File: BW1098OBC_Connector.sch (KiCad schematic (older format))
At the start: 50 parts

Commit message: Cleaned up some duplicates, started reorganizing and putting symbols into one luxonis library so the others can be deleted, added SOM Connector footprint
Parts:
- J?: symbol BW1098OBC_Connector-cache:DF40HC(3.0)-100DS-0.4V_BW1099_G2 -> BW1098OBC_TopLevel-rescue:DF40HC(3.0)-100DS-0.4V_BW1099_G2-BW1098OBC_Connector-cache
- J? (x3): symbol BW1098OBC_Connector-cache:20021121-00010T1LF -> BW1098OBC_TopLevel-rescue:20021121-00010T1LF-BW1098OBC_Connector-cache
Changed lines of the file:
@@
 $Descr B 17000 11000
 encoding utf-8
-Sheet 7 8
+Sheet 6 8
 Title "BW1098OBC_Connector-SchDoc"
 Date "14 12 2020"
@@
 2485_PGOOD and MODULE_nRST both have pull ups to 1.8V \non 1099 module. 2485_PGOOD is held low by open-drain output \non 1099 PMIC until power is good. MODULE_nRST rises with \n1.8V at POR, but can be held low by user button or 1099 JTAG.
 $Comp
-L BW1098OBC_Connector-cache:20021121-00010T1LF J?
+L BW1098OBC_TopLevel-rescue:20021121-00010T1LF-BW1098OBC_Connector-cache J?
 U 1 1 605FCE0C
 P 4250 9550
+AR Path="/605FCE0C" Ref="J?"  Part="1"
+AR Path="/5FD7EFCD/605FCE0C" Ref="J?"  Part="1"
 F 0 "J?" H 4650 9700 60  0000 C CNN
 F 1 "20021121-00010T1LF" H 4800 9000 60  0000 C CNN
@@
 $EndComp
 $Comp
-L BW1098OBC_Connector-cache:20021121-00010T1LF J?
+L BW1098OBC_TopLevel-rescue:20021121-00010T1LF-BW1098OBC_Connector-cache J?
 U 1 1 605FF28B
 P 7150 9550
+AR Path="/605FF28B" Ref="J?"  Part="1"
+AR Path="/5FD7EFCD/605FF28B" Ref="J?"  Part="1"
 F 0 "J?" H 7550 9700 60  0000 C CNN
 F 1 "20021121-00010T1LF" H 7750 9000 60  0000 C CNN
@@
 $EndComp
 $Comp
-L BW1098OBC_Connector-cache:20021121-00010T1LF J?
+L BW1098OBC_TopLevel-rescue:20021121-00010T1LF-BW1098OBC_Connector-cache J?
 U 1 1 6060E6D4
 P 10200 9550
+AR Path="/6060E6D4" Ref="J?"  Part="1"
+AR Path="/5FD7EFCD/6060E6D4" Ref="J?"  Part="1"
 F 0 "J?" H 10650 9700 60  0000 C CNN
 F 1 "20021121-00010T1LF" H 10800 9000 60  0000 C CNN
@@
 	13550 3800 13550 4050
 $Comp
-L BW1098OBC_Connector-cache:DF40HC(3.0)-100DS-0.4V_BW1099_G2 J?
+L BW1098OBC_TopLevel-rescue:DF40HC(3.0)-100DS-0.4V_BW1099_G2-BW1098OBC_Connector-cache J?
 U 1 1 5FDB88CE
 P 7350 2000

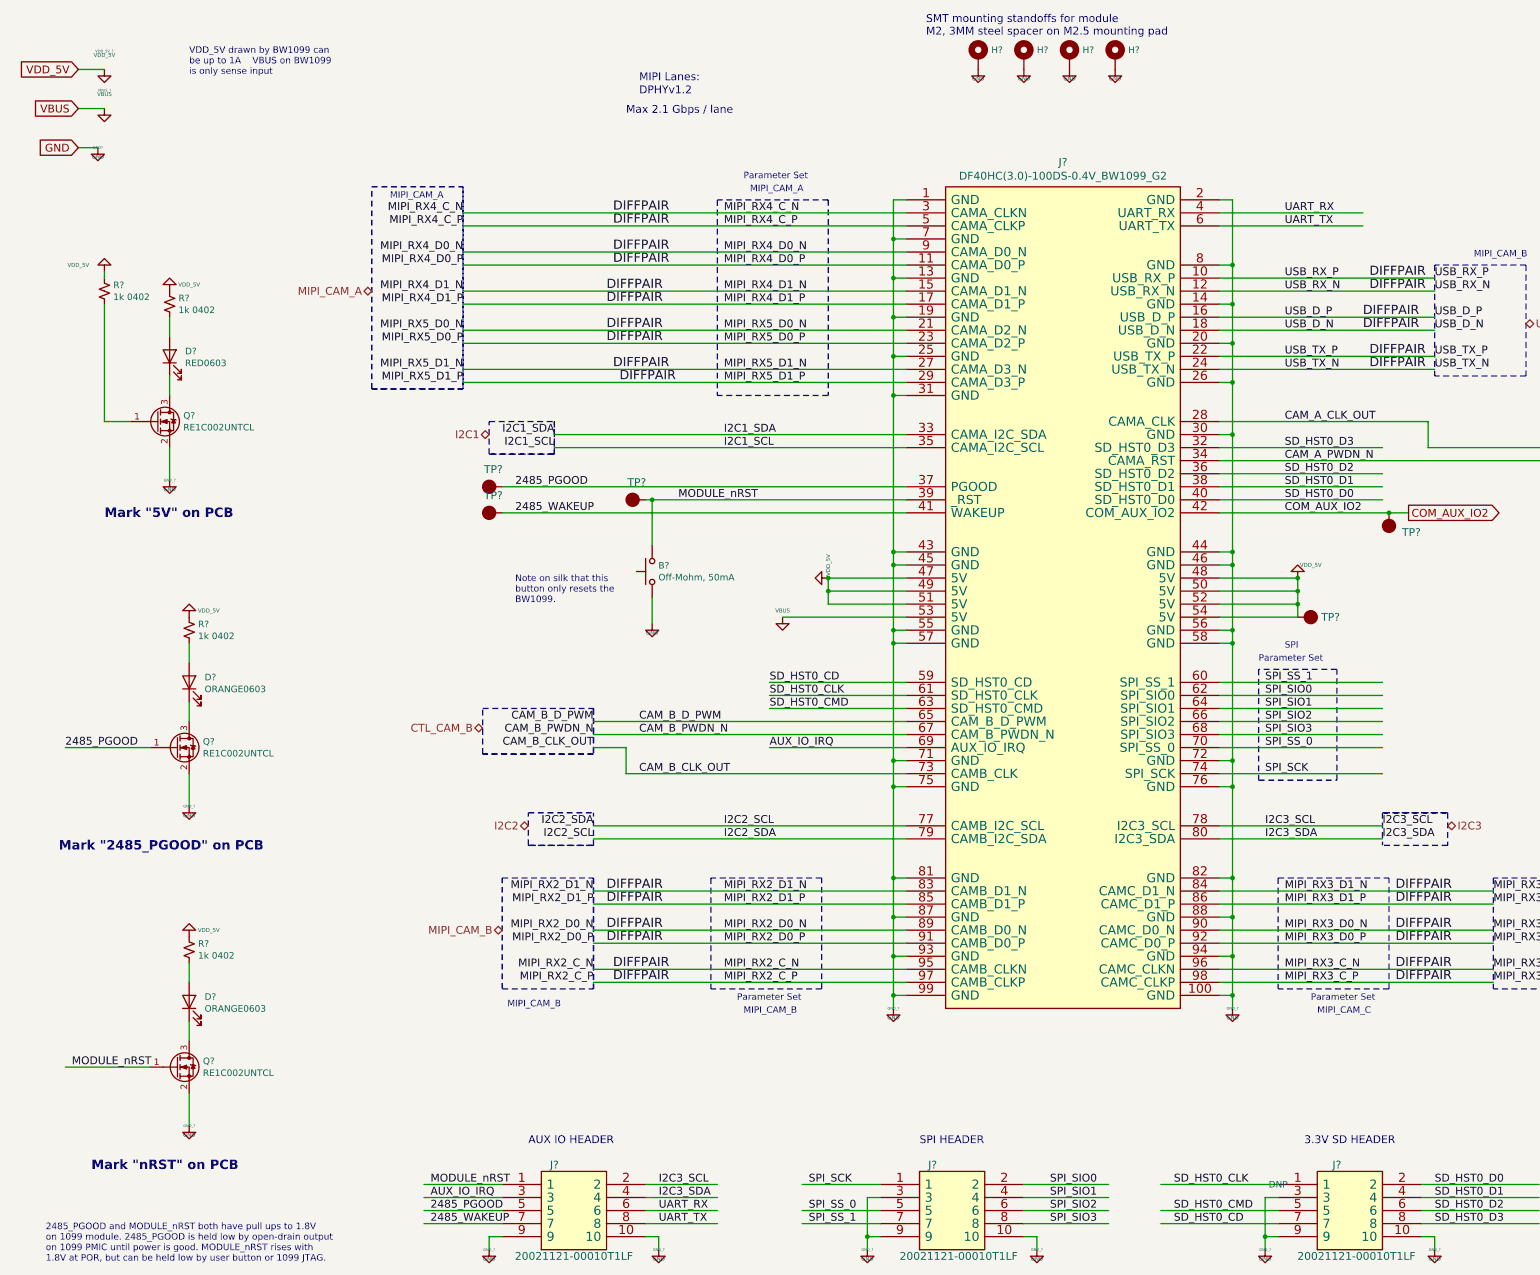
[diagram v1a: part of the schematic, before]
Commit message: More deletion of corrupted or duplicate files, added footprints and associations for mounting holes and 30 pin connector
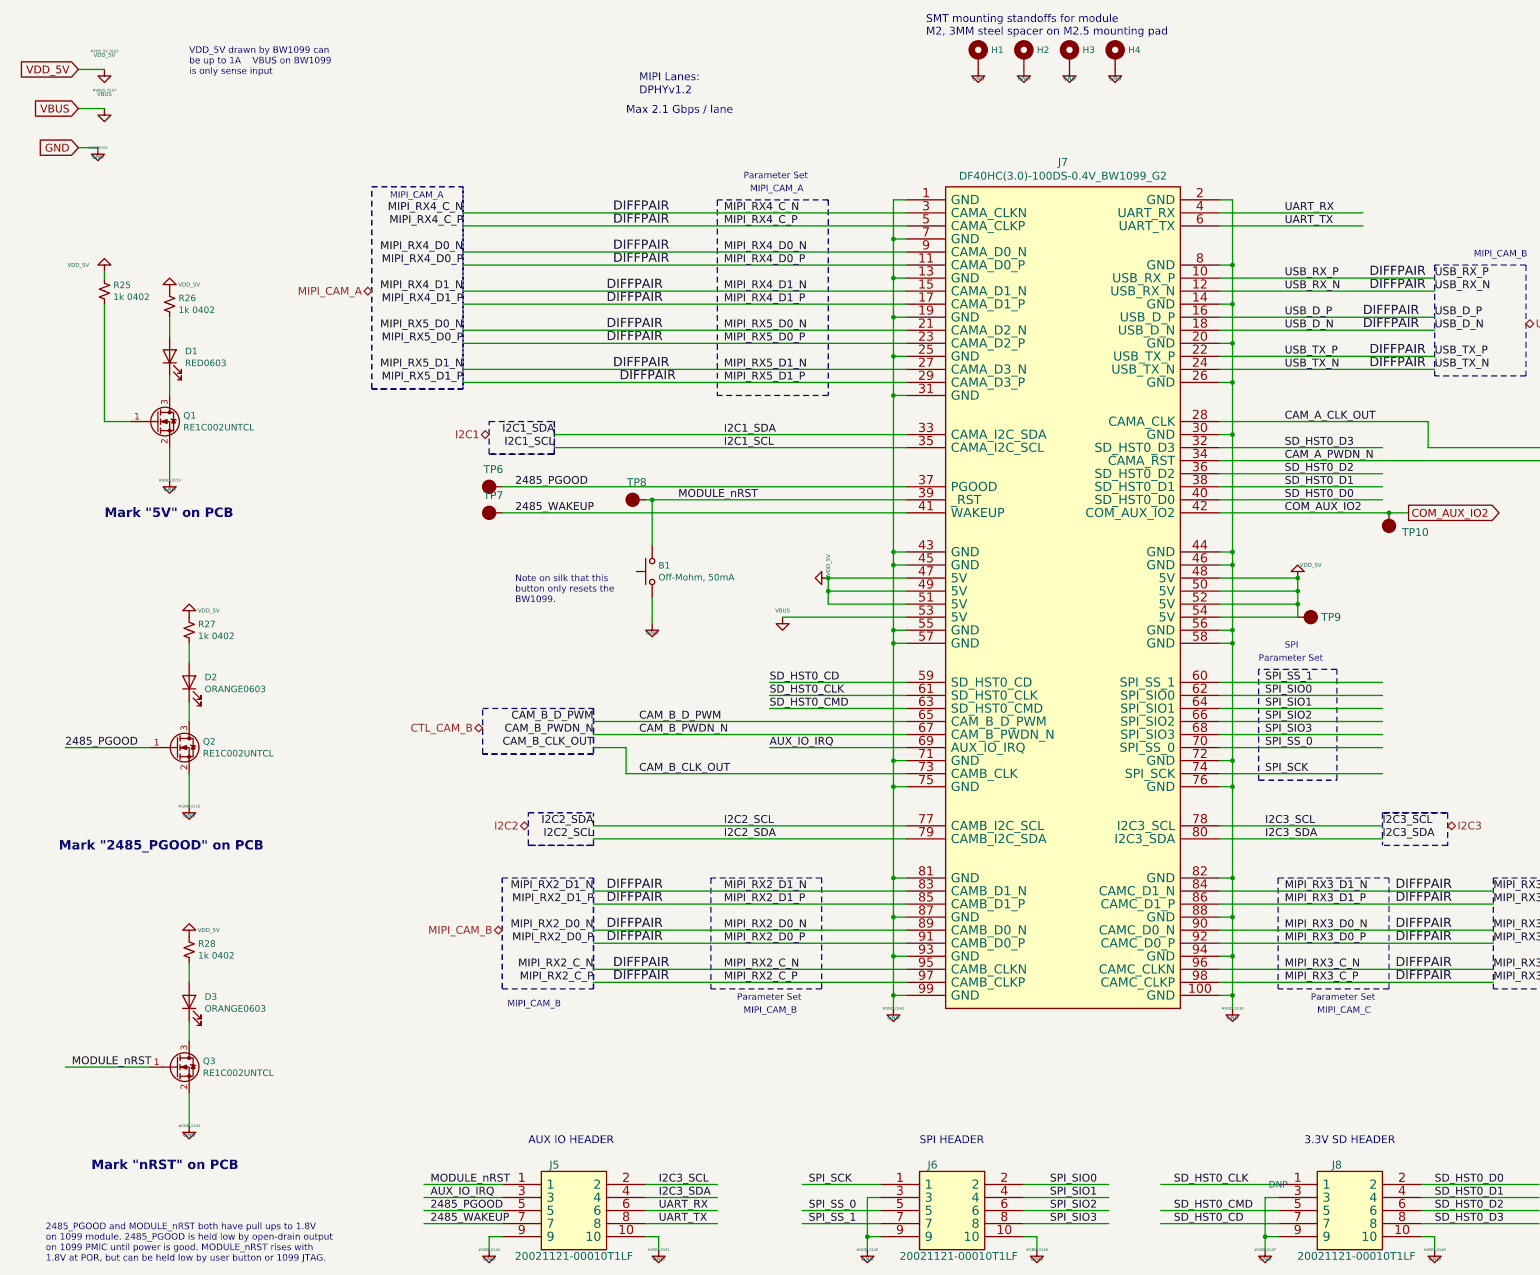
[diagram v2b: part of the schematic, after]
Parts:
- removed GND?, GND_? (x16): GND, symbol power:GND
- removed VBUS?, VBUS_?: VBUS, symbol power:GND
- removed VDD_5V?, VDD_5V_? (x6): VDD_5V, symbol power:GND
- H1, H2, H3, H4: renamed from H?; footprint (none) -> fp_luxonis:Mounting_Wuerth_WA-SMSI-M2_H3mm_9774030243
- J7: renamed from J?; footprint (none) -> fp_luxonis:HRS_DF40HC(3.0)-100DS-0.4V(58
- gave numbers to parts that had none: 19

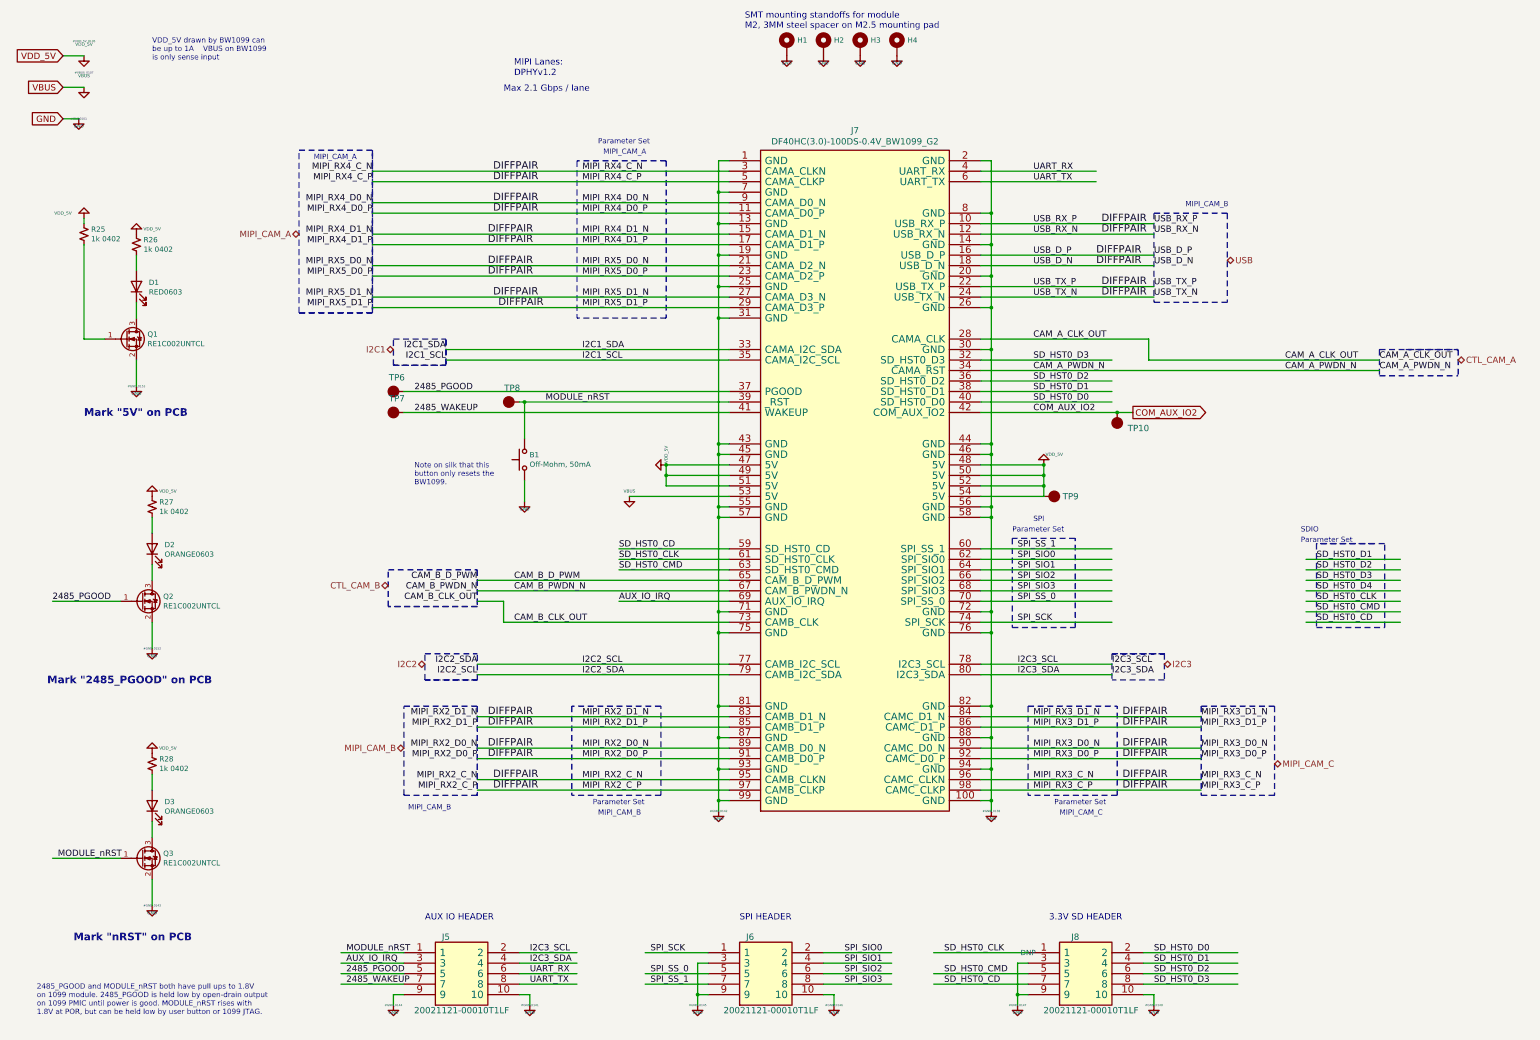
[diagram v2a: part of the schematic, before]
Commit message: fixing labeling and formatting to show proper connections for pcb layout
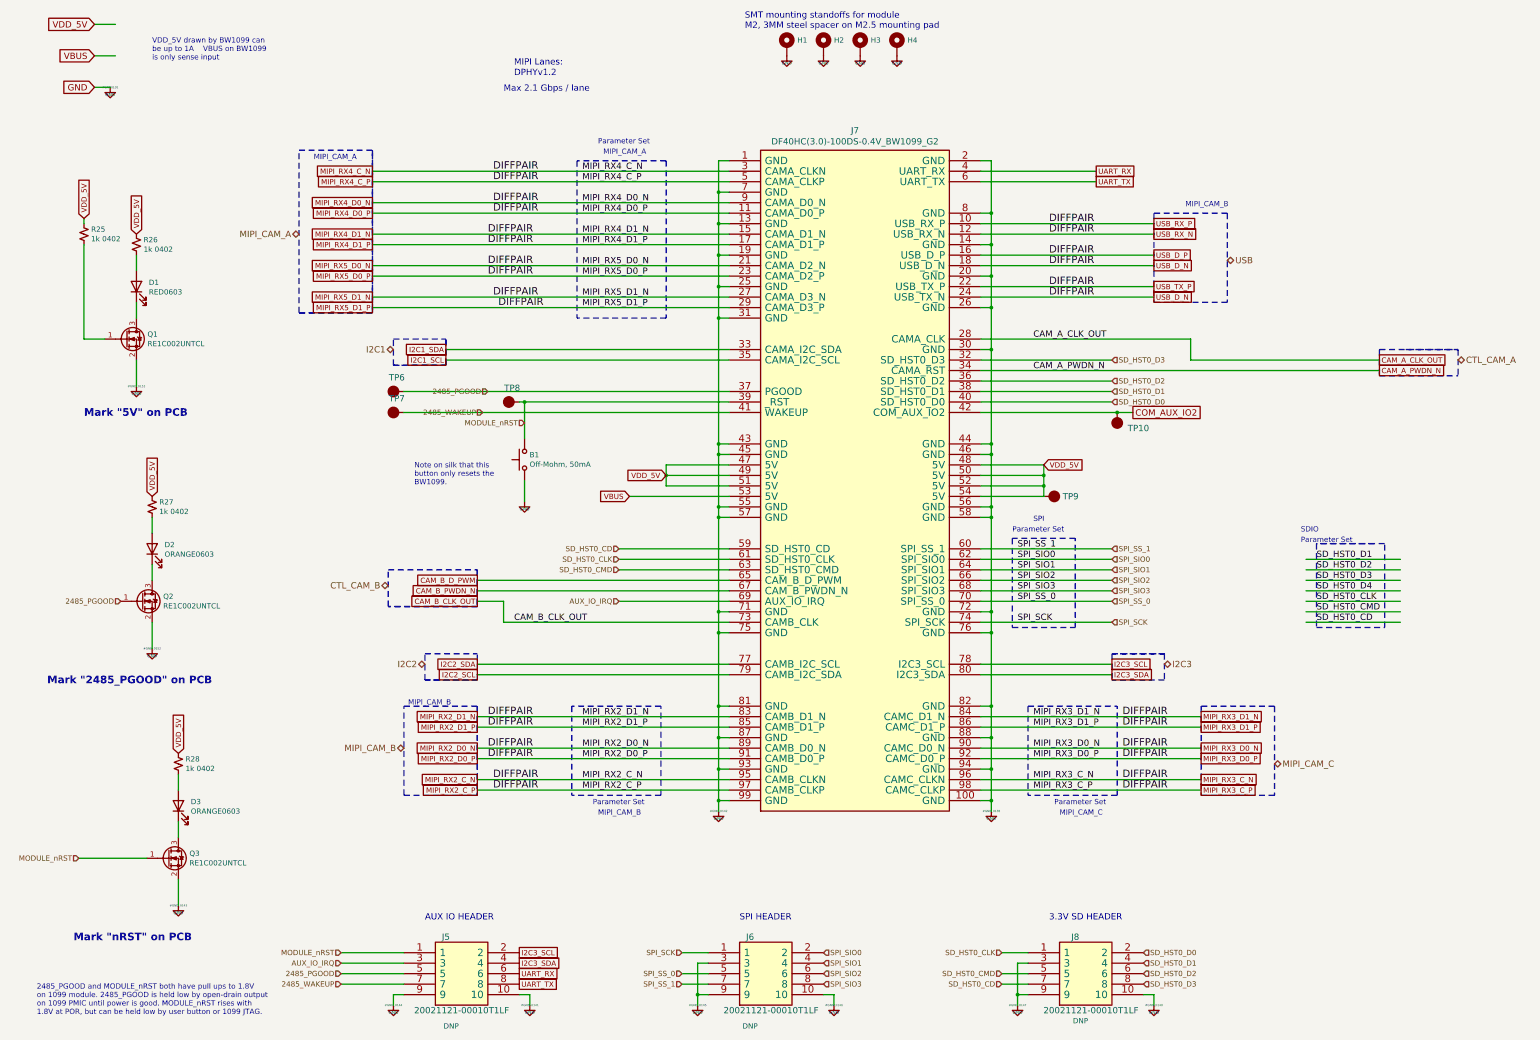
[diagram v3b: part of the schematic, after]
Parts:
- J5, J6: Populated (none) -> DNP
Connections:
- net labels removed: USB_TX_N
- wire segments 207 -> 194
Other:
- moved on the sheet: D3, Q3, R28
